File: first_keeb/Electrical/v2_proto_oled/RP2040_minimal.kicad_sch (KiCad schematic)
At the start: 65 parts, among them P1 USB_C_Receptacle, Q1 BSS138, SW1 SW_Push, SW2 SW_Push, U1 NCP1117-3.3_SOT223, U2 LM4040DBZ-3, U3 W25Q128JVS, U4 RP2040, U5 PRTR5V0U2X, Y1 ABM7-12.000MHZ-D2Y-T

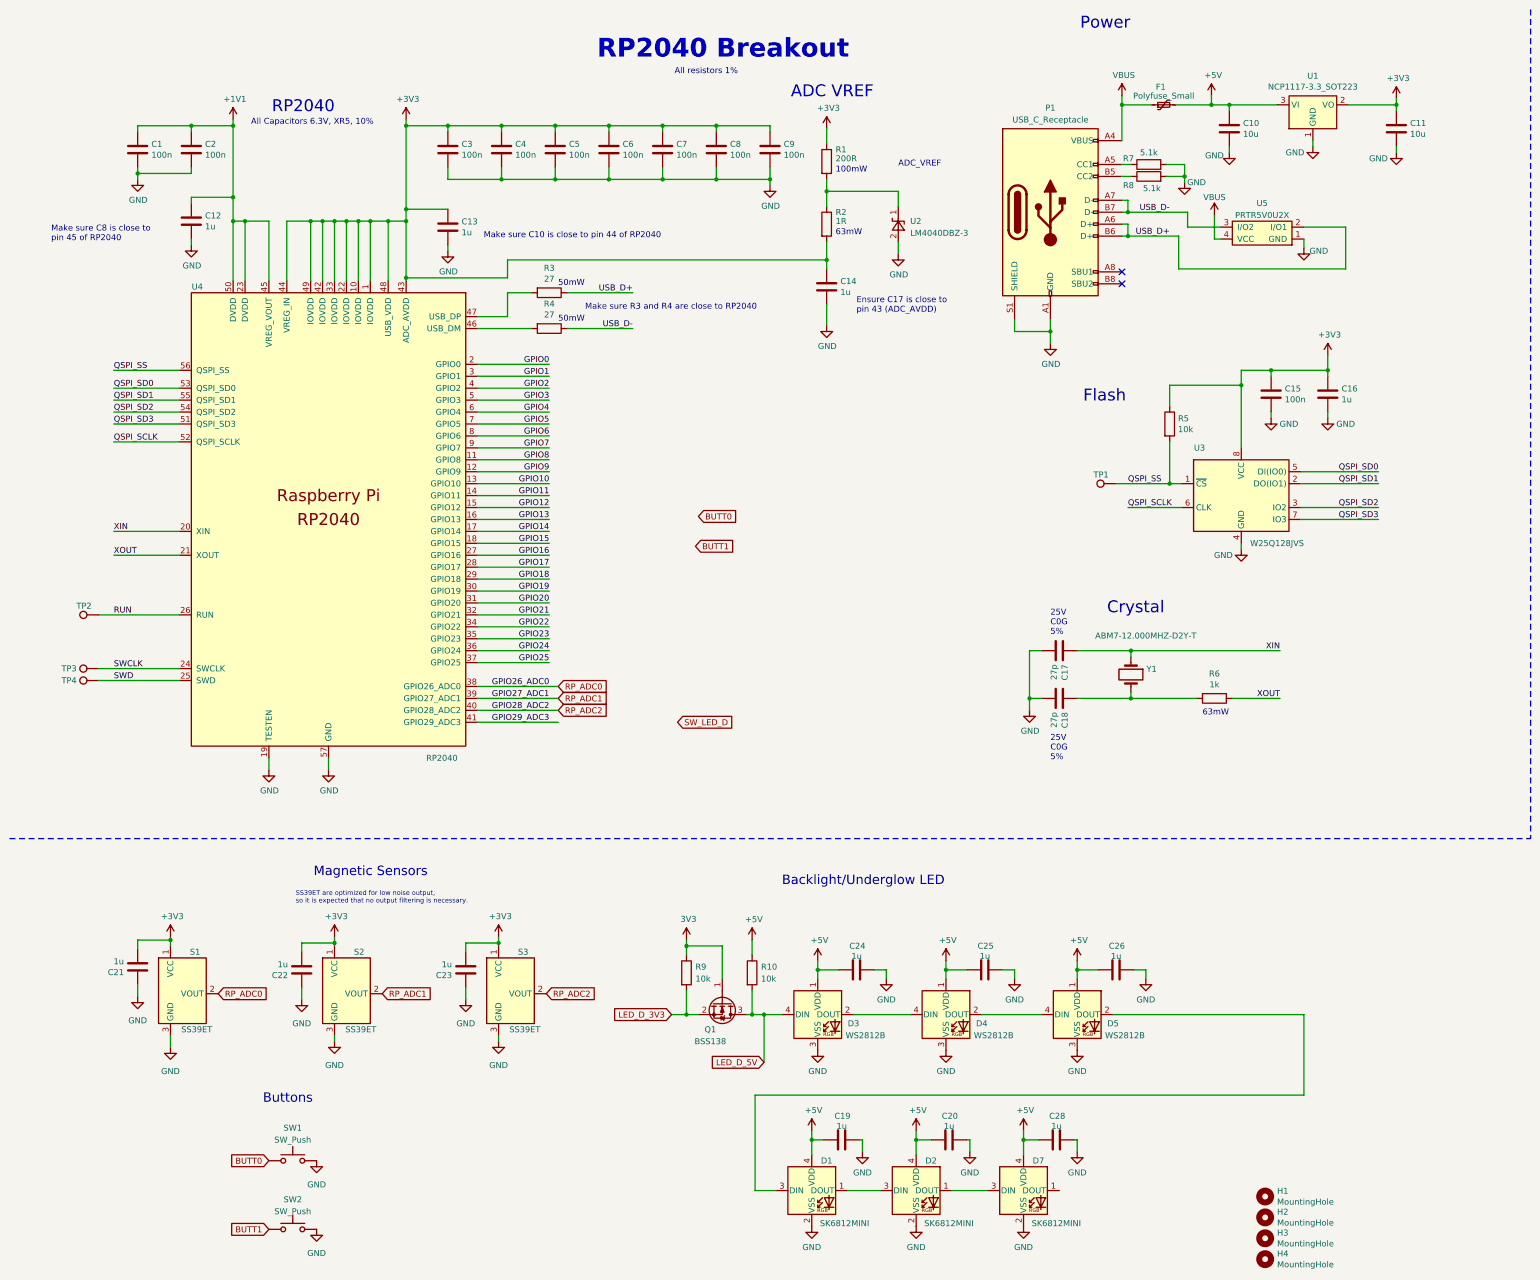
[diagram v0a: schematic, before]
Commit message: finishes pcb except for the test points.
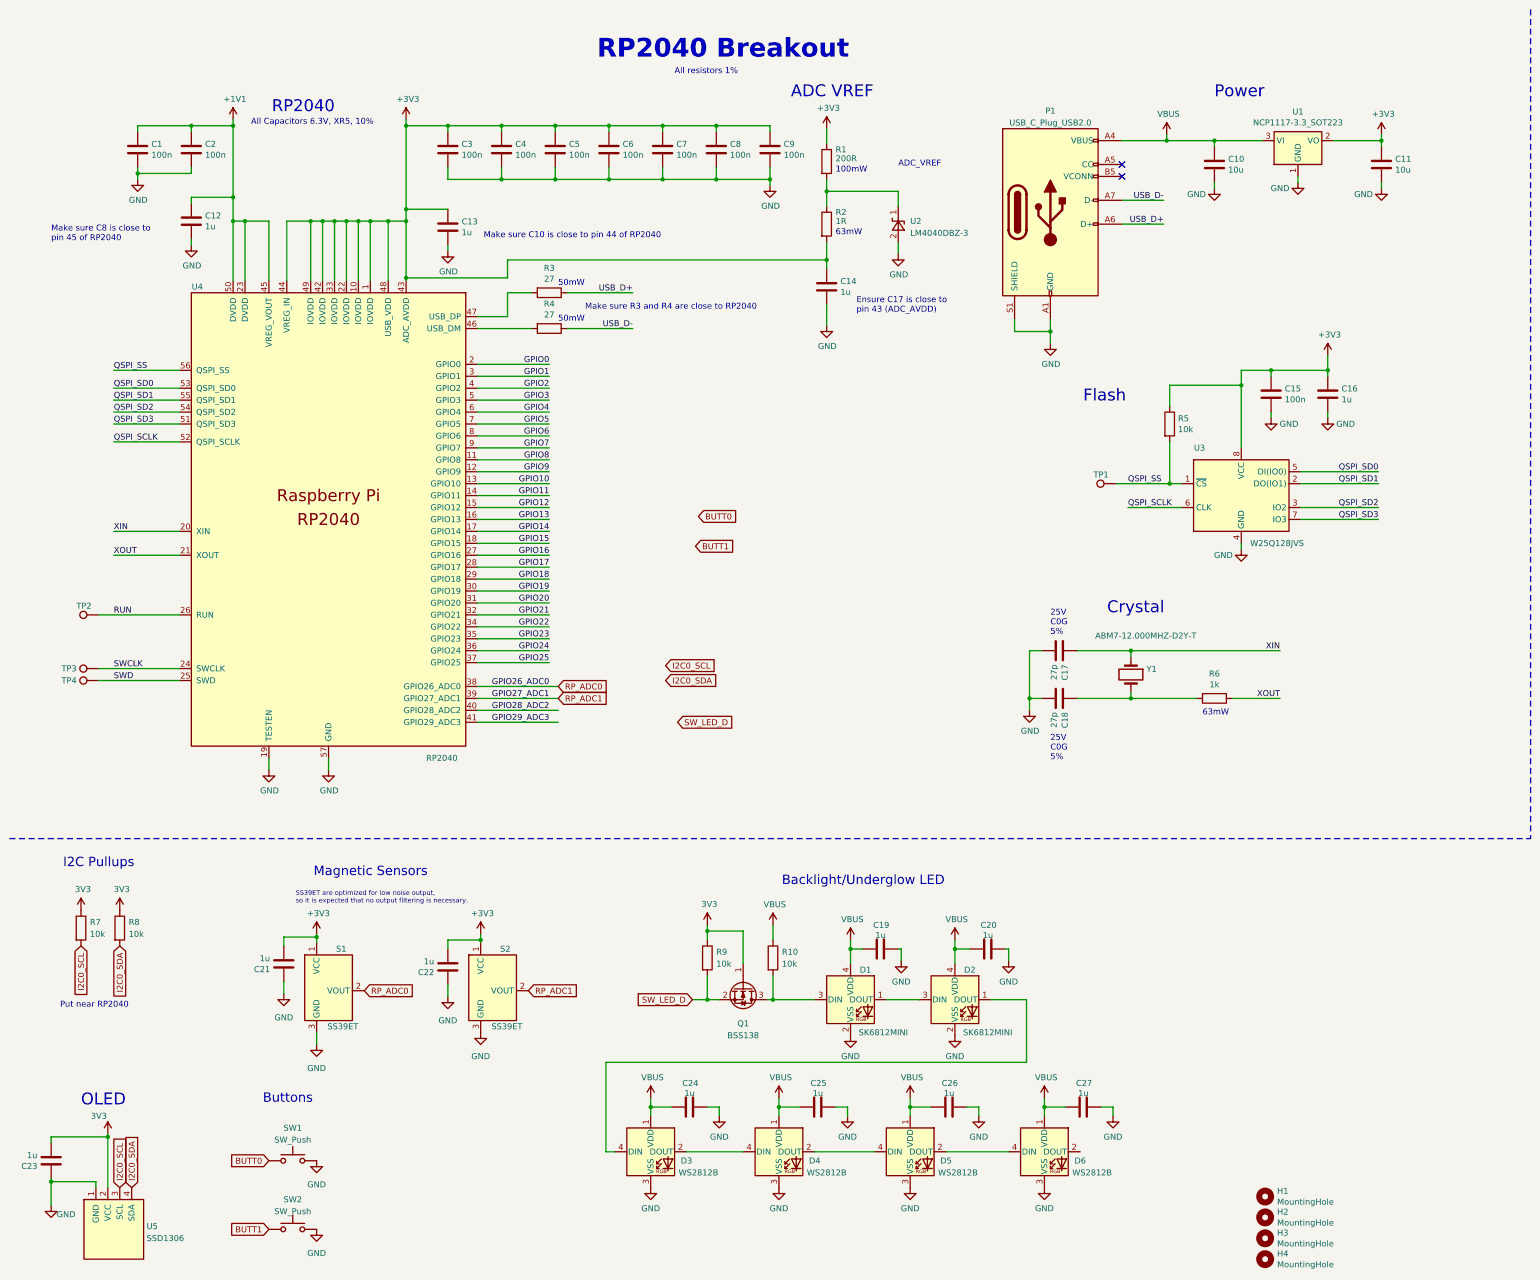
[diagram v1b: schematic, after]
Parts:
- removed C28: 1u, Capacitor_SMD:C_0402_1005Metric, symbol Device:C
- removed D7: SK6812MINI, LED_SMD:LED_SK6812MINI_PLCC4_3.5x3.5mm_P1.75mm, symbol LED:SK6812MINI
- removed F1: Polyfuse_Small, Fuse:Fuse_1206_3216Metric, symbol Device:Polyfuse_Small
- removed S3: SS39ET, Package_TO_SOT_SMD:SOT-23-3, symbol Sensor_Magnetic:SS39ET
- removed U5: PRTR5V0U2X, Package_TO_SOT_SMD:SOT-143, symbol keebio:PRTR5V0U2X
- added C27: 1u, Capacitor_SMD:C_0402_1005Metric, symbol Device:C
- added D6: WS2812B, LED_SMD:LED_WS2812B_PLCC4_5.0x5.0mm_P3.2mm, symbol LED:WS2812B
- added U5: SSD1306, SSD1306:128x64OLED, symbol SSD1306-128x64_OLED:SSD1306
- P1: value USB_C_Receptacle -> USB_C_Plug_USB2.0; symbol Connector:USB_C_Receptacle_USB2.0 -> Connector:USB_C_Plug_USB2.0
- R7, R8: value 5.1k -> 10k
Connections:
- net LED_D_3V3 is gone; now on net SW_LED_D: Q1.2 (S), R9.2
- net +3V3: now also R7.1, R8.1, U5.2 (VCC)
- net GND: now also C23.1, C27.2, D6.3 (VSS), U5.1 (GND); no longer R7.2, R8.2
- net GNDA: no longer C23.1
- net USB_D+: no longer P1.B6 (D+)
- net USB_D-: no longer P1.B7 (D-)
- net VBUS: now also C27.1, D6.1 (VDD)
- net at D2.1 (DOUT): now also D3.4 (DIN)
- net at P1.A5 (CC): no longer R7.1
- net at P1.B5 (VCONN): no longer R8.1
- net at D1.3 (DIN): now also Q1.3 (D), R10.2; no longer D5.2 (DOUT)
- removed net LED_D_5V: D3.4 (DIN), Q1.3 (D), R10.2
- net RP_ADC2 renamed GPIO28_ADC2
- new net: D5.2 (DOUT), D6.4 (DIN)
- new net I2C0_SCL: R7.2, U5.3 (SCL)
- new net I2C0_SDA: R8.2, U5.4 (SDA)
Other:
- note added: "I2C Pullups"
- note added: "OLED"
- note added: "Put near RP2040"
- moved on the sheet: C10, C11, C19, C20, C21, C22, C24, C25, C26, D1, D2, D3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
